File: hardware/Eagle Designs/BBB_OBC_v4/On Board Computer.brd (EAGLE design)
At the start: 90.2 x 95.5 mm, 34 parts, among them J1 MOLEX_503763-0491MOLEX_503763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, J10 503763-0591, J11 503763-0591, J12 503763-0691, J13 MOLEX_503763-0291MOLEX_503763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, J16 U.FL-R-SMT-1(01), J2 MOLEX_503763-0491MOLEX_503763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, J6 MOLEX_503763-0491MOLEX_503763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, J9 U.FL-R-SMT-1(01), P8 SSW-123-02-G-D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

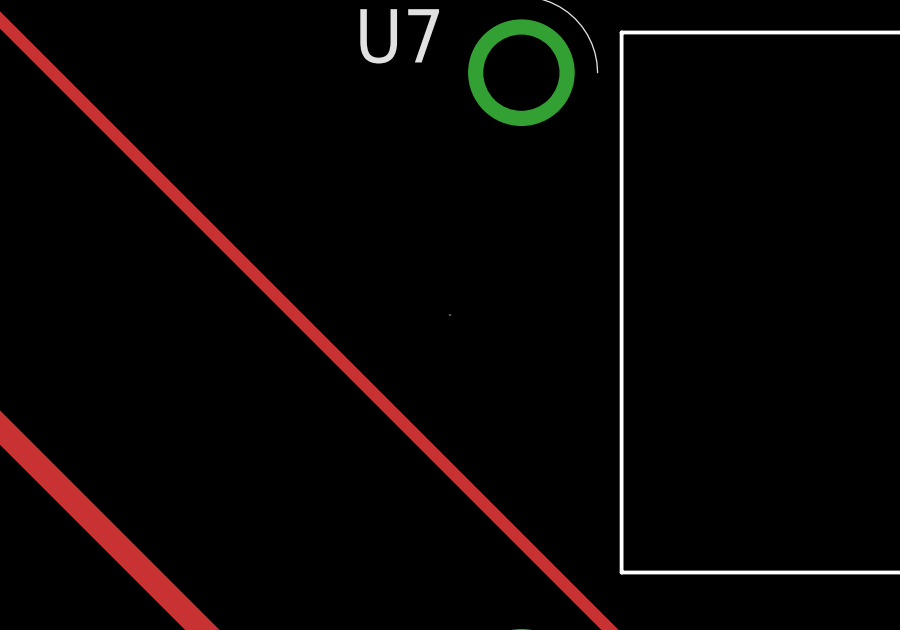
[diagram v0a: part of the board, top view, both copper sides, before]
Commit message: Updated OBC and Solar Panel boards
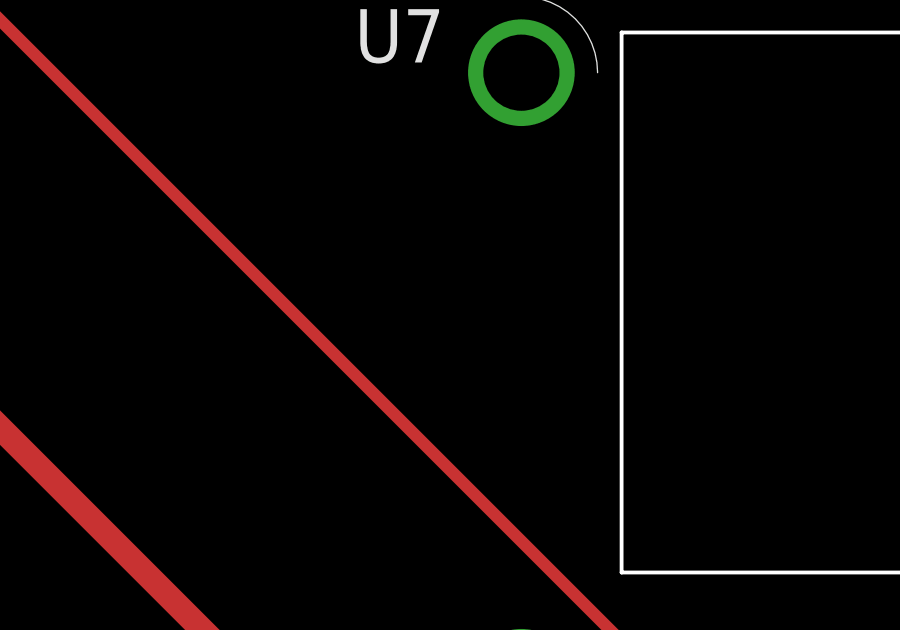
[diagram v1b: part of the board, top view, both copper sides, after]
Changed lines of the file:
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@@
 <rectangle x1="27.1653" y1="30.6705" x2="27.1907" y2="30.6959" layer="21"/>
 <rectangle x1="30.6451" y1="30.6705" x2="30.6959" y2="30.6959" layer="21"/>
-<rectangle x1="60.6421" y1="36.2705" x2="60.7183" y2="36.2959" layer="21"/>
 <rectangle x1="18.1737" y1="30.6705" x2="18.1991" y2="30.6959" layer="21"/>
 <rectangle x1="18.3261" y1="30.6705" x2="18.5547" y2="30.6959" layer="21"/>

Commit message: OBC v4 edits
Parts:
- removed 3V3_BUS, GPS_BOOTSEL: (no value), wirepad:1,6/0,9
- removed GND: GND, wirepad:1,6/0,9
- added L1: L, L:INDC2012X145N
- added R4, R5, R6: 0, HSFL_Main_Library:0805
- X2: device con-samtec:SSW-120-02-G-D -> con-samtec-edited:SSW-120-02-G-D
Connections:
- removed net GPS_BOOTSEL: GPS_BOOTSEL.1, U6.9
- new net N$16: R4.2, R5.2, U6.9
- new net RF_GND: R6.1, U6.21, U6.22, U6.24, U6.25, U6.27, U6.28, U6.29, U6.31, U6.33
- net +3V3_VCC: now also L1.1, U6.58
- net 3V3_BUS: now also R5.1; no longer 3V3_BUS.1
- net GND: now also R4.1, R6.2, U6.10, U6.15, U6.19; no longer GND.1, U6.21
- net N$17: now also L1.2
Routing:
- net 3V3_BUS: track 188.8 -> 103.6 mm
- net GPS_BOOTSEL: track 51.9 -> 0.00 mm
- net RF_GND: track 0.00 -> 16.9 mm
- net N$16: track 0.00 -> 14.6 mm
- net +3V3_VCC: track 130.9 -> 142.8 mm
- net N$17: track 46.6 -> 51.1 mm
- net SPI0_CE1_N: track 39.5 -> 40.1 mm
- net SDA1_I2C: vias 1 -> 0
